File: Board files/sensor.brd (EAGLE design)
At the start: 20.3 x 38.1 mm, 16 parts, among them Q1 2N3904, U1 TL974

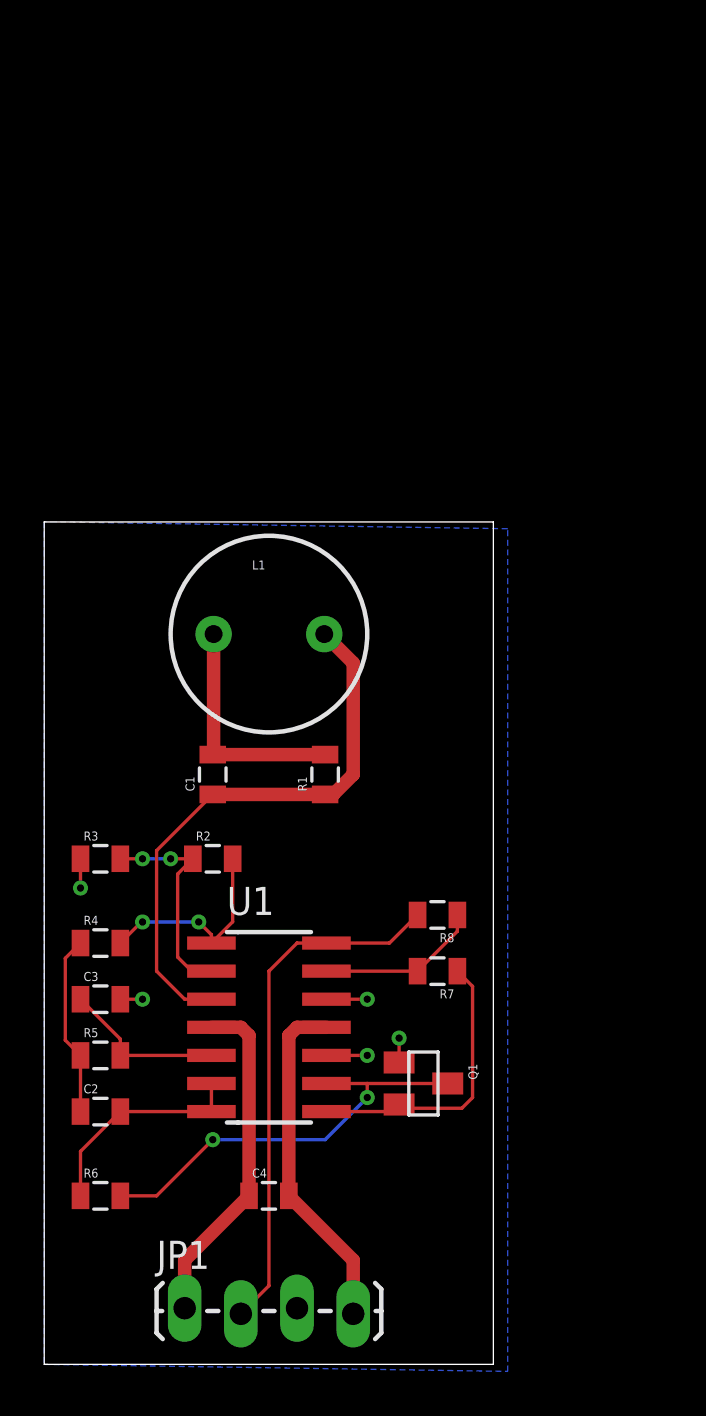
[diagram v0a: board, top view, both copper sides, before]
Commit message: Modified motor driver layout
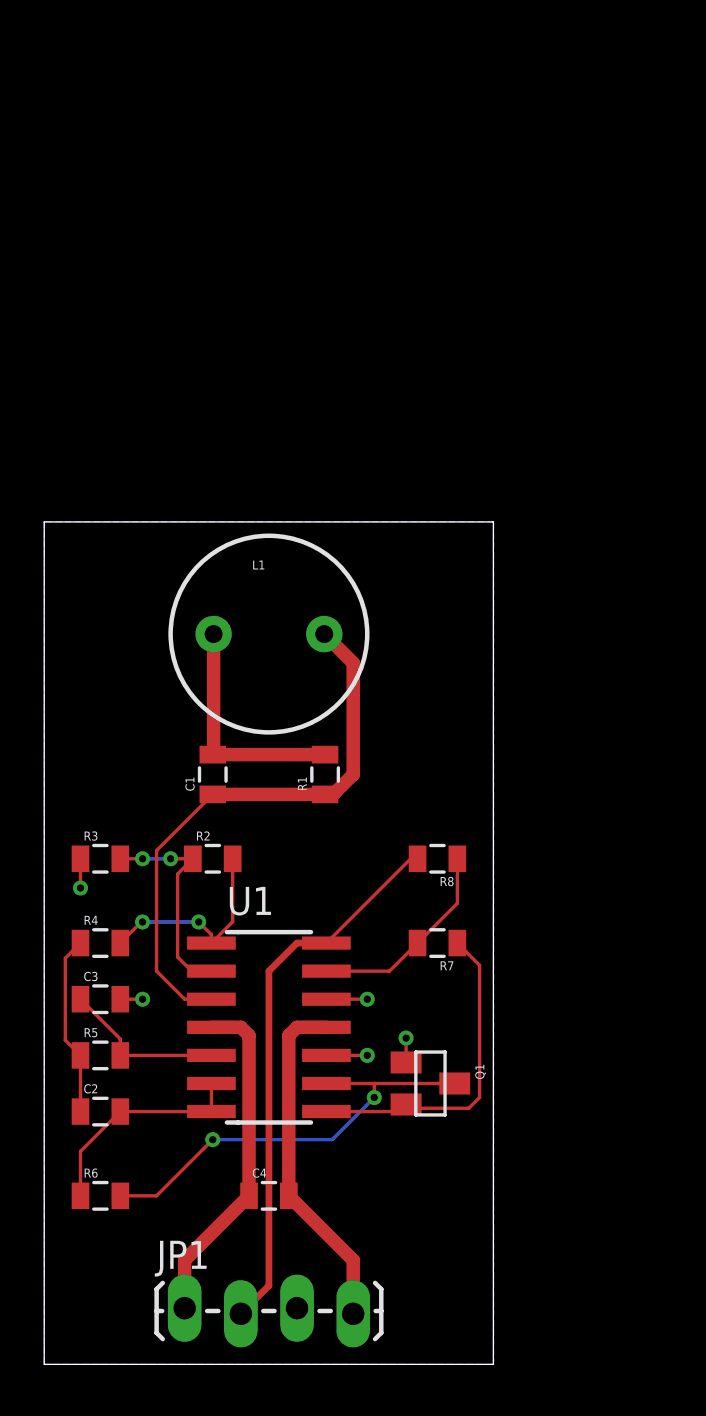
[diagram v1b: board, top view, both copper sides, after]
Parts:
- C2: value (none) -> 300nF
- C3: value (none) -> 150nF
- R4, R5: value (none) -> 10K
- moved R8 2.54 mm to (17.8, 22.9)
- moved R7 1.27 mm to (17.8, 19.1)
- moved Q1 0.32 mm to (17.5, 12.7)
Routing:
- net N$7: track 7.41 -> 9.20 mm
- net N$8: track 13.5 -> 14.9 mm
- net N$11: track 23.8 -> 24.8 mm
- net N$9: track 19.6 -> 20.5 mm
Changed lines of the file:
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@@
 <element name="R2" library="SparkFun-Resistors" package="0805" value="" x="7.62" y="22.86"/>
 <element name="R3" library="SparkFun-Resistors" package="0805" value="" x="2.54" y="22.86"/>
-<element name="R4" library="SparkFun-Resistors" package="0805" value="" x="2.54" y="19.05"/>
-<element name="R5" library="SparkFun-Resistors" package="0805" value="" x="2.54" y="13.97"/>
+<element name="R4" library="SparkFun-Resistors" package="0805" value="10K" x="2.54" y="19.05"/>
+<element name="R5" library="SparkFun-Resistors" package="0805" value="10K" x="2.54" y="13.97"/>
 <element name="R6" library="SparkFun-Resistors" package="0805" value="" x="2.54" y="7.62"/>
-<element name="C2" library="SparkFun-Capacitors" package="0805" value="" x="2.54" y="11.43"/>
-<element name="C3" library="SparkFun-Capacitors" package="0805" value="" x="2.54" y="16.51"/>
-<element name="Q1" library="SparkFun-DiscreteSemi" package="SOT23" value="2N3904" x="17.145" y="12.7" rot="R270"/>
-<element name="R7" library="SparkFun-Resistors" package="0805" value="" x="17.78" y="17.78" rot="R180"/>
-<element name="R8" library="SparkFun-Resistors" package="0805" value="" x="17.78" y="20.32" rot="R180"/>
+<element name="C2" library="SparkFun-Capacitors" package="0805" value="300nF" x="2.54" y="11.43"/>
+<element name="C3" library="SparkFun-Capacitors" package="0805" value="150nF" x="2.54" y="16.51"/>
+<element name="Q1" library="SparkFun-DiscreteSemi" package="SOT23" value="2N3904" x="17.4625" y="12.7" rot="R270"/>
+<element name="R7" library="SparkFun-Resistors" package="0805" value="" x="17.78" y="19.05" rot="R180"/>
+<element name="R8" library="SparkFun-Resistors" package="0805" value="" x="17.78" y="22.86" rot="R180"/>
 </elements>
 <signals>
@@
 <polygon width="0.3048" layer="16">
 <vertex x="0" y="0"/>
-<vertex x="20.955" y="-0.3175"/>
-<vertex x="20.955" y="37.7825"/>
+<vertex x="20.32" y="0"/>
+<vertex x="20.32" y="38.1"/>
 <vertex x="0" y="38.1"/>
 </polygon>
@@
 <wire x1="12.76" y1="13.97" x2="14.605" y2="13.97" width="0.1524" layer="1"/>
 <via x="14.605" y="13.97" extent="1-16" drill="0.3302"/>
-<wire x1="16.045" y1="13.65" x2="16.045" y2="14.7525" width="0.1524" layer="1"/>
-<via x="16.045" y="14.7525" extent="1-16" drill="0.3302"/>
+<wire x1="16.3625" y1="13.65" x2="16.3625" y2="14.7525" width="0.1524" layer="1"/>
+<via x="16.3625" y="14.7525" extent="1-16" drill="0.3302"/>
 <contactref element="U1" pad="12"/>
 <wire x1="12.76" y1="16.51" x2="14.605" y2="16.51" width="0.1524" layer="1"/>
@@
 <contactref element="U1" pad="9"/>
 <contactref element="Q1" pad="3"/>
-<wire x1="18.245" y1="12.7" x2="17.78" y2="12.7" width="0.1524" layer="1"/>
-<wire x1="18.245" y1="12.7" x2="14.605" y2="12.7" width="0.1524" layer="1"/>
-<wire x1="14.605" y1="12.7" x2="12.76" y2="12.7" width="0.1524" layer="1"/>
+<wire x1="18.5625" y1="12.7" x2="17.78" y2="12.7" width="0.1524" layer="1"/>
+<wire x1="18.5625" y1="12.7" x2="14.9225" y2="12.7" width="0.1524" layer="1"/>
+<wire x1="14.9225" y1="12.7" x2="12.76" y2="12.7" width="0.1524" layer="1"/>
 <wire x1="3.44" y1="7.62" x2="5.08" y2="7.62" width="0.1524" layer="1"/>
 <wire x1="5.08" y1="7.62" x2="7.62" y2="10.16" width="0.1524" layer="1"/>
 <via x="7.62" y="10.16" extent="1-16" drill="0.3302"/>
-<wire x1="7.62" y1="10.16" x2="12.7" y2="10.16" width="0.1524" layer="16"/>
-<wire x1="12.7" y1="10.16" x2="14.605" y2="12.065" width="0.1524" layer="16"/>
-<via x="14.605" y="12.065" extent="1-16" drill="0.3302"/>
-<wire x1="14.605" y1="12.065" x2="14.605" y2="12.7" width="0.1524" layer="1"/>
+<wire x1="7.62" y1="10.16" x2="13.0175" y2="10.16" width="0.1524" layer="16"/>
+<wire x1="13.0175" y1="10.16" x2="14.9225" y2="12.065" width="0.1524" layer="16"/>
+<via x="14.9225" y="12.065" extent="1-16" drill="0.3302"/>
+<wire x1="14.9225" y1="12.065" x2="14.9225" y2="12.7" width="0.1524" layer="1"/>
 </signal>
 <signal name="N$11">
@@
 <contactref element="JP1" pad="2"/>
 <contactref element="R8" pad="2"/>
-<wire x1="10.16" y1="3.556" x2="10.16" y2="17.78" width="0.1524" layer="1"/>
-<wire x1="10.16" y1="17.78" x2="11.43" y2="19.05" width="0.1524" layer="1"/>
-<wire x1="11.43" y1="19.05" x2="12.76" y2="19.05" width="0.1524" layer="1"/>
-<wire x1="12.76" y1="19.05" x2="15.61" y2="19.05" width="0.1524" layer="1"/>
-<wire x1="15.61" y1="19.05" x2="16.88" y2="20.32" width="0.1524" layer="1"/>
-<wire x1="8.89" y1="2.286" x2="10.16" y2="3.556" width="0.1524" layer="1"/>
+<wire x1="10.16" y1="3.556" x2="10.16" y2="17.78" width="0.3048" layer="1"/>
+<wire x1="10.16" y1="17.78" x2="11.43" y2="19.05" width="0.3048" layer="1"/>
+<wire x1="11.43" y1="19.05" x2="12.76" y2="19.05" width="0.3048" layer="1"/>
+<wire x1="8.89" y1="2.286" x2="10.16" y2="3.556" width="0.3048" layer="1"/>
+<wire x1="12.76" y1="19.05" x2="16.57" y2="22.86" width="0.1524" layer="1"/>
+<wire x1="16.57" y1="22.86" x2="16.88" y2="22.86" width="0.1524" layer="1"/>
 </signal>
 <signal name="N$8">
 <contactref element="U1" pad="8"/>
 <contactref element="Q1" pad="2"/>
-<wire x1="16.045" y1="11.75" x2="16.51" y2="11.58" width="0.1524" layer="1"/>
+<wire x1="16.3625" y1="11.75" x2="16.51" y2="11.58" width="0.1524" layer="1"/>
 <wire x1="16.51" y1="11.58" x2="16.51" y2="11.43" width="0.1524" layer="1"/>
 <wire x1="16.51" y1="11.43" x2="12.76" y2="11.43" width="0.1524" layer="1"/>
 <contactref element="R7" pad="1"/>
-<wire x1="16.51" y1="11.58" x2="18.8825" y2="11.58" width="0.1524" layer="1"/>
-<wire x1="18.8825" y1="11.58" x2="19.3675" y2="12.065" width="0.1524" layer="1"/>
-<wire x1="19.3675" y1="12.065" x2="19.3675" y2="17.0925" width="0.1524" layer="1"/>
-<wire x1="19.3675" y1="17.0925" x2="18.68" y2="17.78" width="0.1524" layer="1"/>
+<wire x1="16.51" y1="11.58" x2="19.2" y2="11.58" width="0.1524" layer="1"/>
+<wire x1="19.2" y1="11.58" x2="19.685" y2="12.065" width="0.1524" layer="1"/>
+<wire x1="19.685" y1="12.065" x2="19.685" y2="18.045" width="0.1524" layer="1"/>
+<wire x1="19.685" y1="18.045" x2="18.68" y2="19.05" width="0.1524" layer="1"/>
 </signal>
 <signal name="VNEG">
@@
 <contactref element="U1" pad="13"/>
 <contactref element="R8" pad="1"/>
-<wire x1="18.68" y1="20.32" x2="18.68" y2="19.58" width="0.1524" layer="1"/>
-<wire x1="18.68" y1="19.58" x2="16.88" y2="17.78" width="0.1524" layer="1"/>
-<wire x1="16.88" y1="17.78" x2="12.76" y2="17.78" width="0.1524" layer="1"/>
+<wire x1="18.68" y1="22.86" x2="18.68" y2="20.85" width="0.1524" layer="1"/>
+<wire x1="18.68" y1="20.85" x2="16.88" y2="19.05" width="0.1524" layer="1"/>
+<wire x1="16.88" y1="19.05" x2="15.61" y2="17.78" width="0.1524" layer="1"/>
+<wire x1="15.61" y1="17.78" x2="12.76" y2="17.78" width="0.1524" layer="1"/>
 </signal>
 </signals>

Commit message: Significantly modified sensor circuit
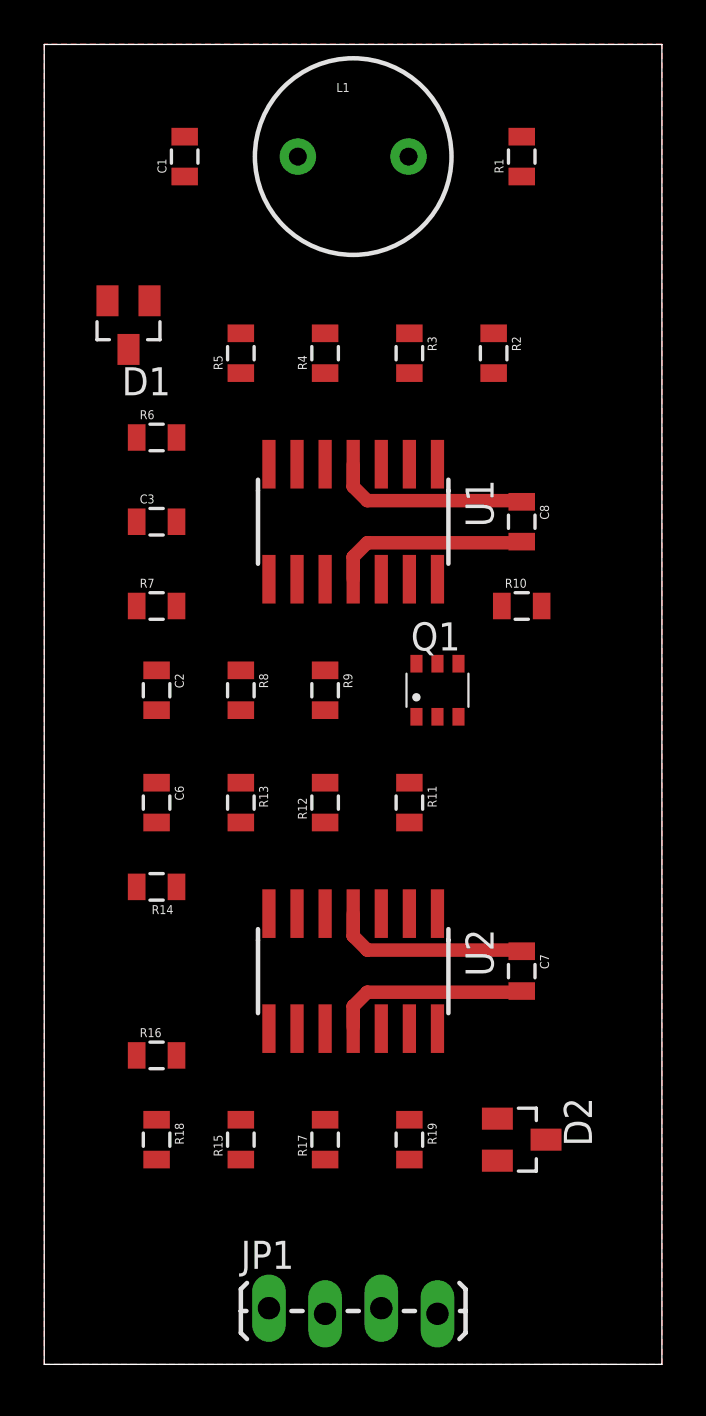
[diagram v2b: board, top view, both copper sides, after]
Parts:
- removed C4: (no value), SparkFun-Capacitors:0805
- added C6: (no value), SparkFun-Capacitors:0805
- added C7, C8: 0.15uF, SparkFun-Capacitors:0805
- added D1, D2: BAS70-04, diode:SOT23
- added R10, R11, R12, R13, R14, R15, R16, R17, R18, R19, R9: (no value), SparkFun-Resistors:0805
- added U2: TL974, Custom:SOIC-14
- C2: value 300nF -> 0.1uF
- C3: value 150nF -> 0.22uF
- Q1: value 2N3904 -> BCM847DS; device SparkFun-DiscreteSemi:SOT23 -> Custom:SOT-457
- R4, R5: value 10K -> (none)
- R6: value (none) -> 10K
- R7: value (none) -> 20K
- U1: device analog-devices:SO14 -> Custom:SOIC-14
- moved R6 34.4 mm to (5.08, 41.9)
- moved R5 32.4 mm to (8.89, 45.7), turned to 90 degrees
- moved R1 29.3 mm to (21.6, 54.6)
- moved R4 28.5 mm to (12.7, 45.7), turned to 90 degrees
- moved C1 28.0 mm to (6.35, 54.6)
- moved R3 26.8 mm to (16.5, 45.7), turned to 270 degrees
- moved R2 26.2 mm to (20.3, 45.7), turned to 270 degrees
- moved U1 23.2 mm to (14.0, 38.1), turned to 180 degrees
- moved L1 21.9 mm to (14.0, 54.6)
- moved C3 21.7 mm to (5.08, 38.1)
- moved R7 19.8 mm to (5.08, 34.3), turned to 0 degrees
- moved C2 19.2 mm to (5.08, 30.5), turned to 270 degrees
- moved Q1 17.8 mm to (17.8, 30.5), turned to 0 degrees
- moved R8 11.7 mm to (8.89, 30.5), turned to 270 degrees
- moved JP1 3.81 mm to (10.2, 2.54)
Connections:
- removed net N$11: JP1.2, R8.2, U1.14
- removed net N$9: Q1.3, R6.2, U1.9
- new net N$10: C3.2, R8.1, U1.8, U1.9
- new net N$13: Q1.6, R8.2, U1.13
- new net N$14: R11.2, U2.1
- new net N$15: Q1.1, Q1.4, R11.1
- new net N$16: Q1.5, R10.1, R9.2
- new net N$17: R14.1, R9.1, U1.14
- new net N$18: C6.1, R12.2, R13.1
- new net N$19: Q1.3, R12.1, U2.2
- new net N$20: R16.2, R17.2, U2.10
- new net N$22: R14.2, R15.1, U2.9
- new net N$23: D2.1, R18.2, R19.1, U2.13
- new net N$24: R15.2, R18.1, U2.8
- new net N$25: D2.3, U2.14
- new net N$26: D2.2, JP1.2, R19.2
- net GND: now also C2.2, C6.2, Q1.2, R10.2, R17.1, U1.5, U2.12, U2.3; no longer C3.2, Q1.1, U1.10
- net N$2: now also D1.1, R4.1, R5.1; no longer C2.2, R6.1, U1.7
- net N$5: now also D1.2, R6.1; no longer C3.1, U1.5
- net N$6: now also R7.2, U1.10; no longer R4.1, R5.1
- net N$7: now also C3.1, R6.2, R7.1; no longer R7.2, R8.1, U1.13
- net N$8: now also D1.3, U1.7; no longer Q1.2, R7.1, U1.8
- net VCC: now also C7.1, C8.1, R13.2, R16.1, U2.4; no longer C4.1
- net VNEG: now also C7.2, C8.2, U2.11; no longer C4.2
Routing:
- net N$1: track 25.7 -> 0.00 mm
- net N$11: track 24.8 -> 0.00 mm
- net N$9: track 20.5 -> 0.00 mm, vias 2 -> 0
- net GND: track 18.0 -> 0.00 mm, vias 5 -> 0
- net N$8: track 14.9 -> 0.00 mm
- net N$2: track 9.95 -> 0.00 mm
- net N$3: track 9.80 -> 0.00 mm, vias 2 -> 0
- net N$4: track 9.34 -> 0.00 mm, vias 2 -> 0
- net N$7: track 9.20 -> 0.00 mm
- net N$6: track 8.19 -> 0.00 mm
- net N$5: track 7.41 -> 0.00 mm
- net VCC: track 15.4 -> 17.8 mm
- net VNEG: track 15.6 -> 17.8 mm
- added copper zone on layer 1, net GND
- removed copper zone on layer 16, net GND
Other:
- board size 20.3 x 38.1 mm -> 27.9 x 59.7 mm

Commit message: Finished new sensor board layout
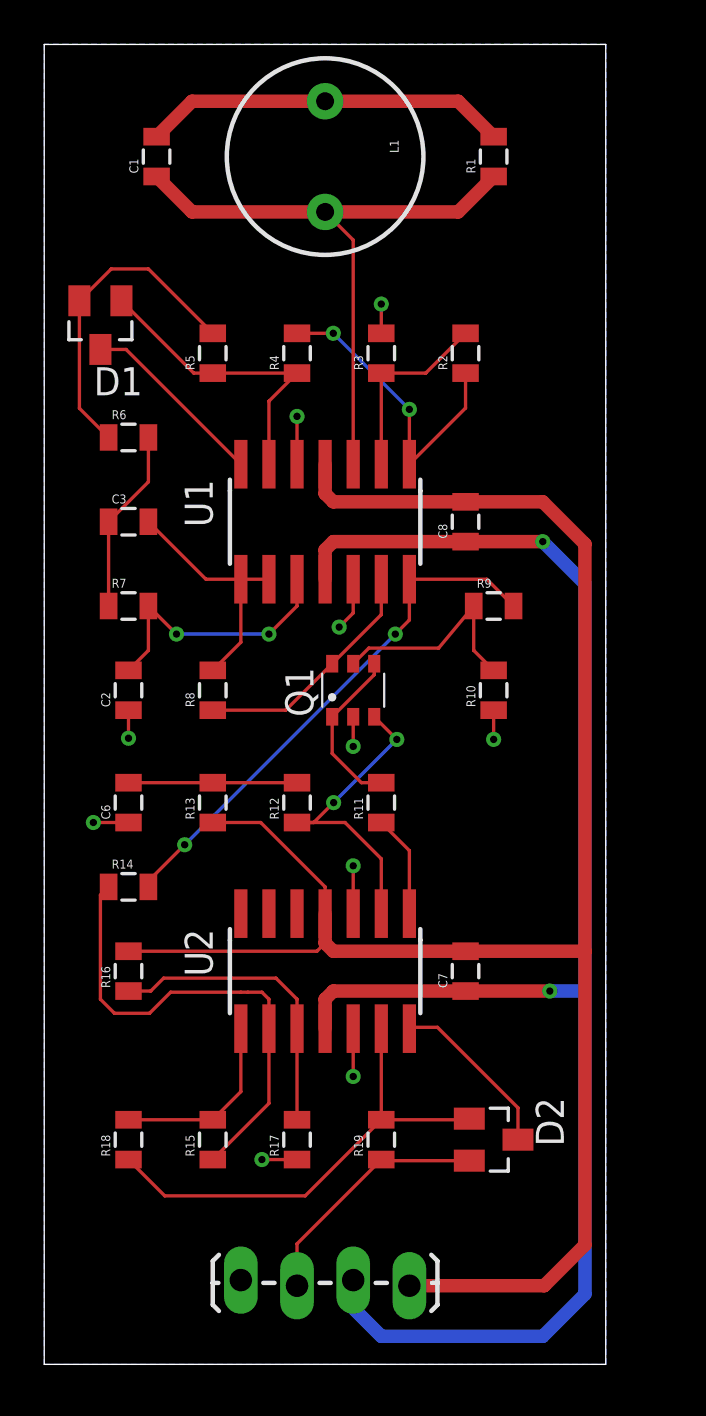
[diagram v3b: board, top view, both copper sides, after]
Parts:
- moved R9 8.52 mm to (20.3, 34.3), turned to 0 degrees
- moved R16 4.02 mm to (3.81, 17.8), turned to 90 degrees
- moved R10 4.02 mm to (20.3, 30.5), turned to 90 degrees
- moved Q1 3.81 mm to (14.0, 30.5)
- moved C7 2.54 mm to (19.1, 17.8), turned to 90 degrees
- moved C8 2.54 mm to (19.1, 38.1), turned to 90 degrees
- moved JP1 1.80 mm to (8.89, 3.81)
- moved L1 1.27 mm to (12.7, 54.6), turned to 270 degrees
- moved R11 1.27 mm to (15.2, 25.4), turned to 90 degrees
- moved R19 1.27 mm to (15.2, 10.2), turned to 90 degrees
- moved R3 1.27 mm to (15.2, 45.7), turned to 90 degrees
- moved U1 1.27 mm to (12.7, 38.1)
- moved U2 1.27 mm to (12.7, 17.8)
- moved R13 1.27 mm to (7.62, 25.4), turned to 90 degrees
- moved R15 1.27 mm to (7.62, 10.2)
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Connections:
- net GND: now also C2.1, C6.1, JP1.1, R10.1, R3.2; no longer C2.2, C6.2, JP1.3, R10.2, R3.1
- net N$10: now also R8.2; no longer R8.1
- net N$13: now also R8.1; no longer R8.2
- net N$14: now also R11.1; no longer R11.2
- net N$15: now also R11.2; no longer R11.1
- net N$16: now also R10.2, R9.1; no longer R10.1, R9.2
- net N$17: now also R14.2, R9.2; no longer R14.1, R9.1
- net N$18: now also C6.2, R13.2; no longer C6.1, R13.1
- net N$20: now also R16.1; no longer R16.2
- net N$22: now also R14.1; no longer R14.2
- net N$23: now also R18.1, R19.2; no longer R18.2, R19.1
- net N$24: now also R18.2; no longer R18.1
- net N$26: now also R19.1; no longer R19.2
- net N$3: now also R2.2, R3.1; no longer R2.1, R3.2
- net N$4: now also R2.1; no longer R2.2
- net N$6: now also C2.2; no longer C2.1
- net VCC: now also C7.2, C8.2, JP1.4, R13.1, R16.2; no longer C7.1, C8.1, JP1.1, R13.2, R16.1
- net VNEG: now also C7.1, C8.1, JP1.3; no longer C7.2, C8.2, JP1.4
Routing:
- net VCC: track 17.8 -> 84.2 mm
- net VNEG: track 17.8 -> 72.4 mm, vias 0 -> 2
- net GND: track 0.00 -> 33.9 mm, vias 0 -> 10
- net N$1: track 0.00 -> 28.5 mm
- net N$17: track 0.00 -> 24.0 mm, vias 0 -> 2
- net N$22: track 0.00 -> 21.9 mm
- net N$23: track 0.00 -> 21.7 mm
- net N$5: track 0.00 -> 14.6 mm
- net N$19: track 0.00 -> 14.5 mm, vias 0 -> 2
- net N$4: track 0.00 -> 14.2 mm, vias 0 -> 2
- net N$2: track 0.00 -> 13.9 mm
- net N$20: track 0.00 -> 13.7 mm
- net N$6: track 0.00 -> 12.3 mm, vias 0 -> 2
- net N$26: track 0.00 -> 11.3 mm
- net N$10: track 0.00 -> 11.2 mm
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- added copper zone on layer 16, net GND
- removed copper zone on layer 1, net GND
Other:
- board size 27.9 x 59.7 mm -> 25.4 x 59.7 mm
